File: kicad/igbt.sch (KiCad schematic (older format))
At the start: 40 parts, among them J801 Screw_Terminal_01x15, J802 Screw_Terminal_01x15, U801 SI8660BD, U802 SI8662BD, U803 SN74LVC2G17DBVR, U804 SN74LVC2G17DBVR, U805 SN74LVC2G17DBVR, U806 SN74LVC2G17DBVR, U807 SN74LVC2G17DBVR, U808 SN74LVC2G17DBVR, U809 SN74LVC2G17DBVR, U810 SN74LVC2G17DBVR, U811 SN74LVC2G17DBVR, U812 SN74LVC2G17DBVR, U813 SI8660BD, U814 SI8662BD

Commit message: I've passed all footprin to layout BUT...
I've passed all, first glance... I need to confirm in details a lot of
things. The objetive for these is to have an aproximation of the size
I'll need to make the board.. then I choose the final detailed footprint
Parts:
- removed J801, J802: Screw_Terminal_01x15, symbol Connector:Screw_Terminal_01x15
- added C801, C802, C803, C804, C805, C806, C807, C808, C809, C810, C811, C812, C813, C814, C815, C816, C817, C818, C819, C820, C821, C822, C823, C824: 10p, servo:C_0603_1608Metric, symbol servo:Capacitor
- U801, U802, U813, U814: footprint (none) -> Package_SO:SOIC-16W_7.5x10.3mm_P1.27mm
- U803, U804, U805, U806, U807, U808, U809, U810, U811, U812: footprint (none) -> servo:SOT-23-6
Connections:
- net GNDH: now also C801.1, C802.1, C803.1, C804.1, C805.1, C806.1, C807.1, C808.1, C809.1, C810.1, C811.1, C812.1, C813.1, C814.1, C815.1, C816.1, C817.1, C818.1, C819.1, C820.1, C821.1, C822.1, C823.1, C824.1
- net PWM_A_1H_H: now also R801.2, C818.2 (Capacitor); no longer R801.1, U803.6 (1Y)
- net PWM_A_1L_H: now also R802.2, C816.2 (Capacitor); no longer R802.1, U803.4 (2Y)
- net PWM_A_2H_H: now also R803.2, C814.2 (Capacitor); no longer R803.1, U804.6 (1Y)
- net PWM_A_2L_H: now also R804.2, C812.2 (Capacitor); no longer R804.1, U804.4 (2Y)
- net PWM_A_3H_H: now also R805.2, C810.2 (Capacitor); no longer R805.1, U805.6 (1Y)
- net PWM_A_3L_H: now also R806.2, C808.2 (Capacitor); no longer R806.1, U805.4 (2Y)
- net PWM_A_BRK_RES_H: now also R807.2, C806.2 (Capacitor); no longer R807.1, U806.6 (1Y)
- net PWM_B_1H_H: now also R813.1, C807.2 (Capacitor); no longer R813.2, U808.6 (1Y)
- net PWM_B_1L_H: now also R814.1, C809.2 (Capacitor); no longer R814.2, U808.4 (2Y)
- net PWM_B_2H_H: now also R815.1, C811.2 (Capacitor); no longer R815.2, U809.6 (1Y)
- net PWM_B_2L_H: now also R816.1, C813.2 (Capacitor); no longer R816.2, U809.4 (2Y)
- net PWM_B_3H_H: now also R817.1, C815.2 (Capacitor); no longer R817.2, U810.6 (1Y)
- net PWM_B_3L_H: now also R818.1, C817.2 (Capacitor); no longer R818.2, U810.4 (2Y)
- net PWM_B_BRK_RES_H: now also R819.1, C819.2 (Capacitor); no longer R819.2, U811.6 (1Y)
- net BRK_A_MEC_H: now reaches R808.2
- net BRK_A_MEC_H: now also C805.2 (Capacitor)
- net FREE_OUT_A1_H: now reaches R809.2
- net FREE_OUT_A1_H: now also C804.2 (Capacitor)
- net FREE_OUT_A2_H: now reaches R810.2
- net FREE_OUT_A2_H: now also C803.2 (Capacitor)
- net at R811.1, U802.11 (B5): now also C802.2 (Capacitor)
- net FREE_IN_A3_H: now reaches R811.2
- net at R812.1, U802.10 (B6): now also C801.2 (Capacitor)
- net FREE_IN_A4_H: now reaches R812.2
- net BRK_B_MEC_H: now reaches R820.1
- net BRK_B_MEC_H: now also C820.2 (Capacitor)
- net FREE_OUT_B1_H: now reaches R821.1
- net FREE_OUT_B1_H: now also C821.2 (Capacitor)
- net FREE_OUT_B2_H: now reaches R822.1
- net FREE_OUT_B2_H: now also C822.2 (Capacitor)
- net FREE_IN_B3_H: now reaches R823.1
- net at R823.2, U814.11 (B5): now also C823.2 (Capacitor)
- net FREE_IN_B4_H: now reaches R824.1
- net at R824.2, U814.10 (B6): now also C824.2 (Capacitor)
- net PWM_A_BRK_MEC_H: no longer names the net of R808.1, U806.4 (2Y)
- net PWM_B_BRK_MEC_H: no longer names the net of R820.2, U811.4 (2Y)
- new net: R807.1, U806.6 (1Y)
- new net: R806.1, U805.4 (2Y)
- new net: R805.1, U805.6 (1Y)
- new net: R804.1, U804.4 (2Y)
- new net: R803.1, U804.6 (1Y)
- new net: R802.1, U803.4 (2Y)
- new net: R801.1, U803.6 (1Y)
- new net: R819.2, U811.6 (1Y)
- new net: R818.2, U810.4 (2Y)
- new net: R817.2, U810.6 (1Y)
- new net: R816.2, U809.4 (2Y)
- new net: R815.2, U809.6 (1Y)
- new net: R814.2, U808.4 (2Y)
- new net: R813.2, U808.6 (1Y)
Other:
- note added: "PWM OUT -> ISOLATOR -> BUFFER -> FILTER\n"
- note added: "these pins has isolation and a buffer. They could be directly connected\n to a IGBT module for test porpouses or to a power board and another\n isolation stage for production porpouses to have a reinforced isolation.\n In next stages of the development of the board, the buffers could be\n eliminated, but not the isolation Scmith trigger stage\n\nI left other multiporpouse IN/OUT using the free \n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"
- note removed: "PWM OUT -> ISOLATOR -> BUFFER -> LED"
- note removed: "is an optionally 15vh out if the\n power board wanna use it"
- note removed: "these pins has isolation and a buffer. They could be directly connected\n to a IGBT module for test porpouses or to a power board and another\n isolation stage for production porpouses to have a reinforced isolation.\n In next stages of the development of the board, the buffers could be\n eliminated, but not the isolation Scmith trigger stage"

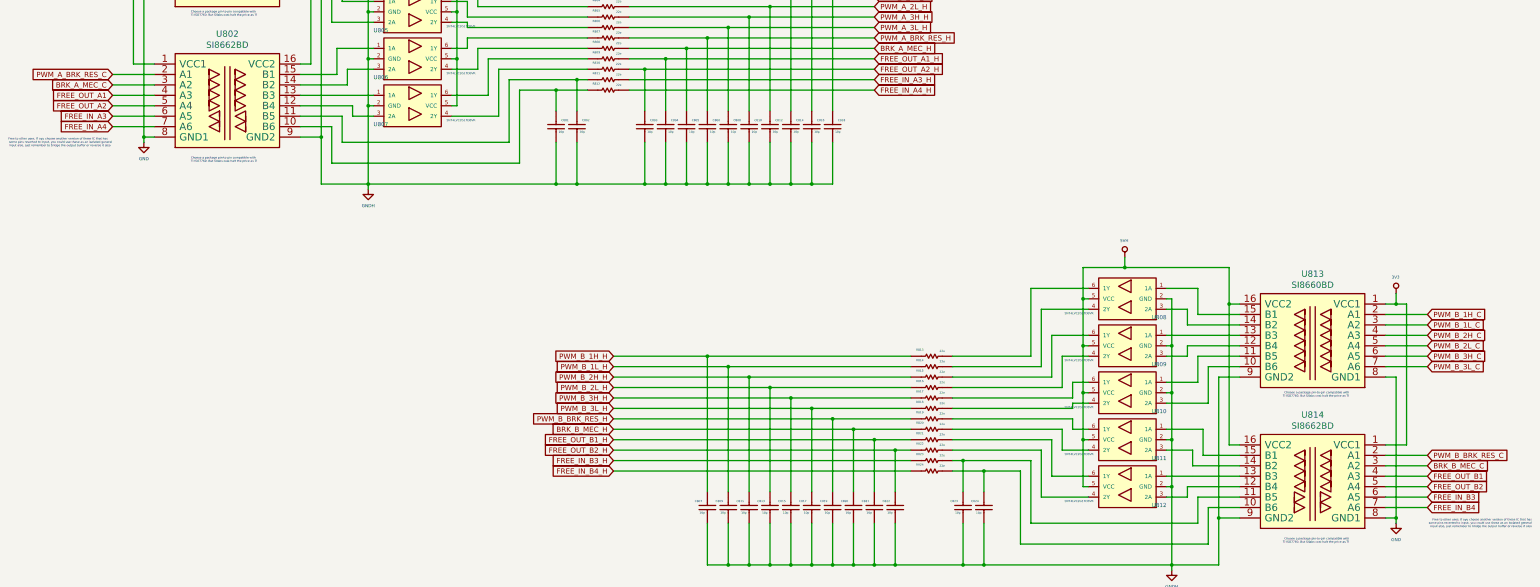
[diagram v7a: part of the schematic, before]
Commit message: I forgot that QUEP was diferential!! all to back....
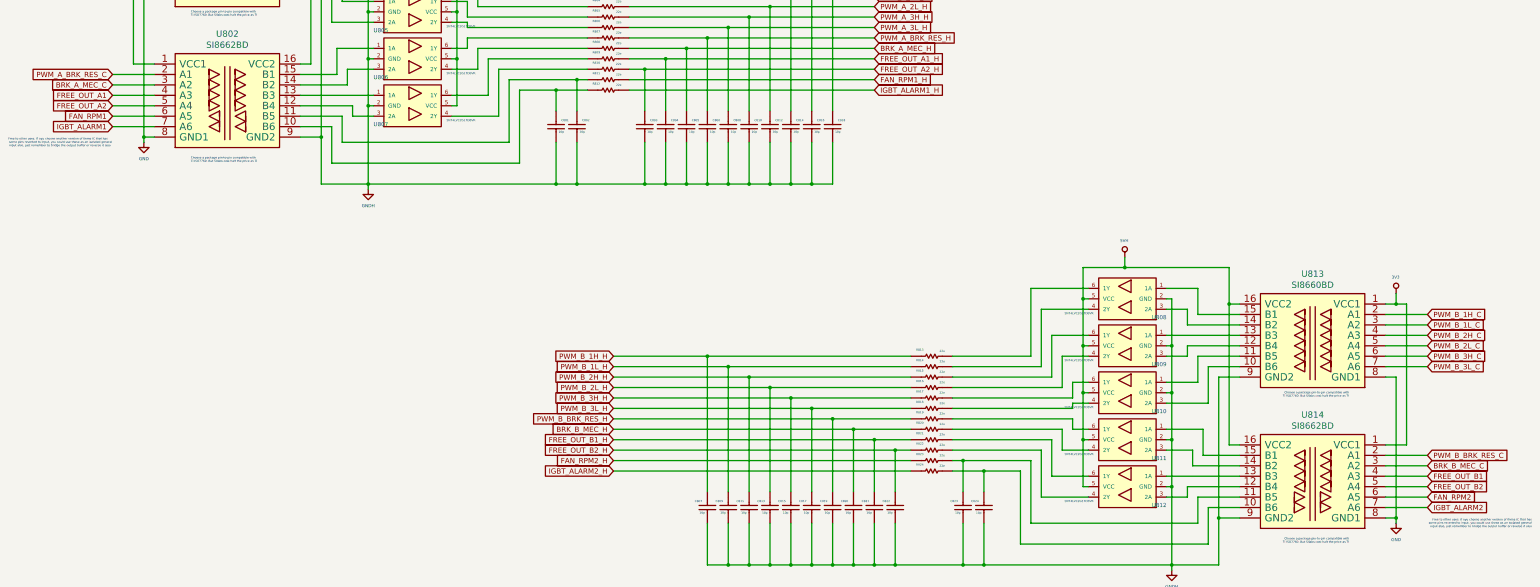
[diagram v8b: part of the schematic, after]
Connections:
- net FREE_IN_A3 renamed FAN_RPM1
- net FREE_IN_A3_H renamed FAN_RPM1_H
- net FREE_IN_A4 renamed IGBT_ALARM1
- net FREE_IN_A4_H renamed IGBT_ALARM1_H
- net FREE_IN_B3 renamed FAN_RPM2
- net FREE_IN_B3_H renamed FAN_RPM2_H
- net FREE_IN_B4 renamed IGBT_ALARM2
- net FREE_IN_B4_H renamed IGBT_ALARM2_H
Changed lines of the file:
@@
 $Descr A3 16535 11693
 encoding utf-8
-Sheet 8 18
+Sheet 8 19
 Title "Igbt interface"
 Date "2020-01-09"
@@
 Text GLabel 14550 7400 2    50   Input ~ 0
 FREE_OUT_B2
-Text GLabel 14550 7500 2    50   Input ~ 0
-FREE_IN_B3
-Text GLabel 14550 7600 2    50   Input ~ 0
-FREE_IN_B4
 Text GLabel 14550 7200 2    50   Input ~ 0
 BRK_B_MEC_C
@@
 Text GLabel 1950 3750 0    50   Input ~ 0
 FREE_OUT_A2
-Text GLabel 1950 3850 0    50   Input ~ 0
-FREE_IN_A3
-Text GLabel 1950 3950 0    50   Input ~ 0
-FREE_IN_A4
 Wire Wire Line
 	2350 3650 1950 3650
@@
 F 3 "../doc/datasheets/sn74lvc2g17.pdf" H 4650 2950 60  0001 C CNN
 	1    4950 2500
-	1    0    0    -1
-$EndComp
-$Comp
-L servo:SN74LVC2G17DBVR U803
-U 1 1 5E60CBFC
-P 4950 2050
-F 0 "U803" H 4450 1950 39  0000 L BNN
-F 1 "SN74LVC2G17DBVR" H 5150 2000 20  0000 L BNN
-F 2 "servo:SOT-23-6" H 4450 2250 60  0001 C CNN
-F 3 "../doc/datasheets/sn74lvc2g17.pdf" H 4650 2500 60  0001 C CNN
-	1    4950 2050
 	1    0    0    -1
 $EndComp
@@
 Text GLabel 6750 7050 0    50   Input ~ 0
 FREE_OUT_B2_H
-Text GLabel 6750 7150 0    50   Input ~ 0
-FREE_IN_B3_H
-Text GLabel 6750 7250 0    50   Input ~ 0
-FREE_IN_B4_H
 Text GLabel 9250 2500 2    50   Input ~ 0
 PWM_A_1H_H
@@
 Text GLabel 9250 3400 2    50   Input ~ 0
 FREE_OUT_A2_H
+$Comp
+L servo:SN74LVC2G17DBVR U803
+U 1 1 5E60CBFC
+P 4950 2050
+F 0 "U803" H 4450 1950 39  0000 L BNN
+F 1 "SN74LVC2G17DBVR" H 5150 2000 20  0000 L BNN
+F 2 "servo:SOT-23-6" H 4450 2250 60  0001 C CNN
+F 3 "../doc/datasheets/sn74lvc2g17.pdf" H 4650 2500 60  0001 C CNN
+	1    4950 2050
+	1    0    0    -1
+$EndComp
+Text GLabel 1950 3850 0    50   Input ~ 0
+FAN_RPM1
+Text GLabel 1950 3950 0    50   Input ~ 0
+IGBT_ALARM1
 Text GLabel 9250 3500 2    50   Input ~ 0
-FREE_IN_A3_H
+FAN_RPM1_H
 Text GLabel 9250 3600 2    50   Input ~ 0
-FREE_IN_A4_H
+IGBT_ALARM1_H
+Text GLabel 6750 7150 0    50   Input ~ 0
+FAN_RPM2_H
+Text GLabel 6750 7250 0    50   Input ~ 0
+IGBT_ALARM2_H
+Text GLabel 14550 7500 2    50   Input ~ 0
+FAN_RPM2
+Text GLabel 14550 7600 2    50   Input ~ 0
+IGBT_ALARM2
 $EndSCHEMATC
